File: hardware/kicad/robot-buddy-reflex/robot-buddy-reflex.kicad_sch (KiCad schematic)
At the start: 23 parts, among them J1 Motor A, J2 Motor B, J5 Qwiic, J6 HC-SR04, J7 E-Stop, J8 PWR In, J9 UART/Pi, U1 Waveshare_ESP32-S3-Zero, U2 SparkFun_TB6612FNG_v2

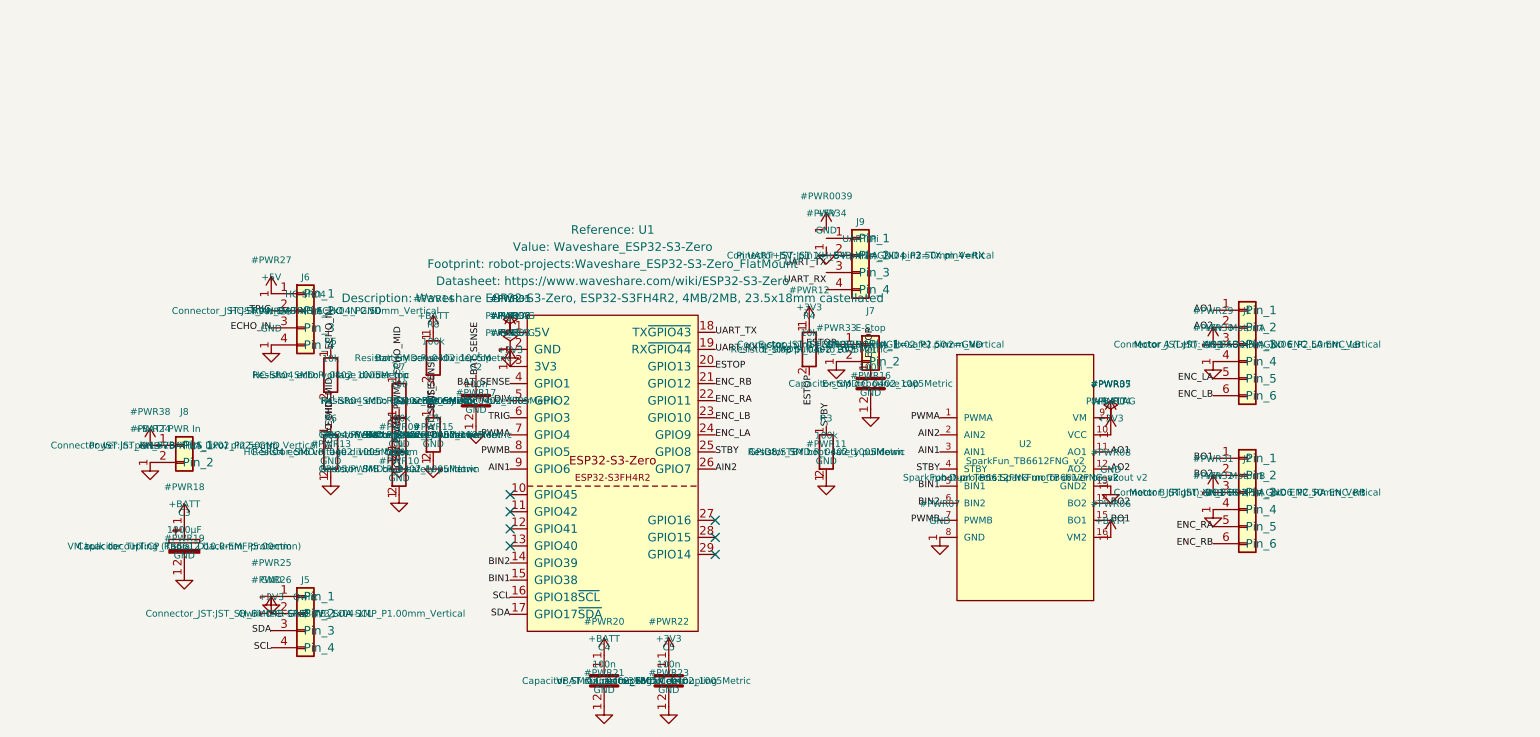
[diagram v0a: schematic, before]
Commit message: schematic: add J10 power LED, J11 NeoPixel, U3 level-shift circuit
J10 (XH 2-pin): panel-mount power LED hardwired to +5V rail via R10
(330Ω) — always on when powered, no GPIO dependency.

J11 (XH 3-pin): WS2812B NeoPixel DATA/+5V/GND. Data driven by GPIO42
(inner cluster pad 11) through U3 (74LVC1G125 SOT-23-5), which
level-shifts 3.3V→5V to meet WS2812B Vih. R11 (330Ω) suppresses
ringing on the 800kHz data line. C6 (100µF) + C7 (100nF) decouple the
5V rail at the connector against 64-LED inrush.
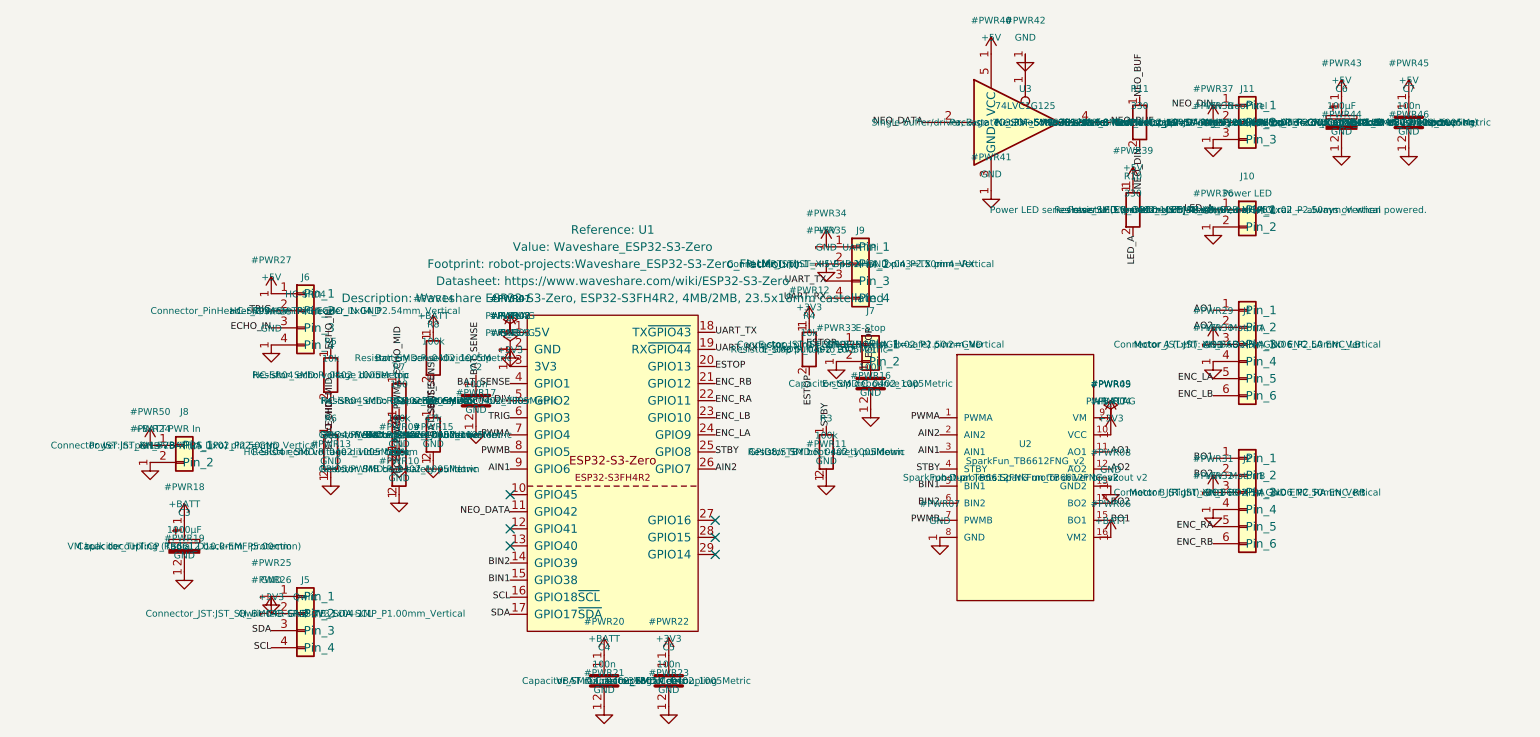
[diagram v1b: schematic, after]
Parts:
- added C6: 100µF, Capacitor_THT:CP_Radial_D5.0mm_P2.50mm, symbol Device:C_Polarized
- added C7: 100n, Capacitor_SMD:C_0402_1005Metric, symbol Device:C
- added J10: Power LED, Connector_JST:JST_XH_B2B-XH-A_1x02_P2.50mm_Vertical, symbol Connector_Generic:Conn_01x02
- added J11: NeoPixel, Connector_JST:JST_XH_B3B-XH-A_1x03_P2.50mm_Vertical, symbol Connector_Generic:Conn_01x03
- added R10, R11: 330, Resistor_SMD:R_0402_1005Metric, symbol Device:R
- added U3: 74LVC1G125, Package_TO_SOT_SMD:SOT-23-5, symbol 74xGxx:74LVC1G125
- J6: footprint Connector_JST:JST_XH_B4B-XH-A_1x04_P2.50mm_Vertical -> Connector_PinHeader_2.54mm:PinHeader_1x04_P2.54mm_Vertical
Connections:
- net +5V: now also J9.1 (Pin_1), C6.1, C7.1, J11.2 (Pin_2), R10.1, U3.5 (VCC)
- net GND: now also J9.2 (Pin_2), C6.2, C7.2, J10.2 (Pin_2), J11.3 (Pin_3), U3.1, U3.3 (GND)
- net UART_RX: now also J9.4 (Pin_4)
- net UART_TX: now also J9.3 (Pin_3)
- net NEO_DATA: now reaches U1.11 (GPIO42)
- net NEO_DATA: now also U3.2
- new net LED_A: J10.1 (Pin_1), R10.2
- new net NEO_BUF: R11.1, U3.4
- new net NEO_DIN: J11.1 (Pin_1), R11.2
- no-connect marks 7 -> 6

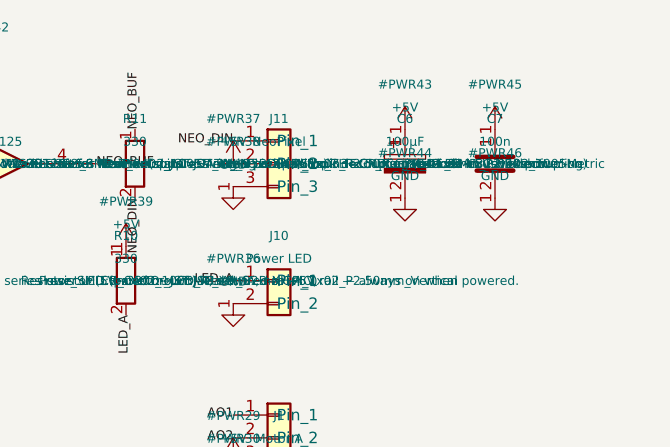
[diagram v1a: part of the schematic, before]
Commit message: hardware: fix C6 NeoPixel bulk cap footprint to P2.00mm
EEU-FM1A101 has 2.00mm lead spacing; P2.50mm would have been wrong.
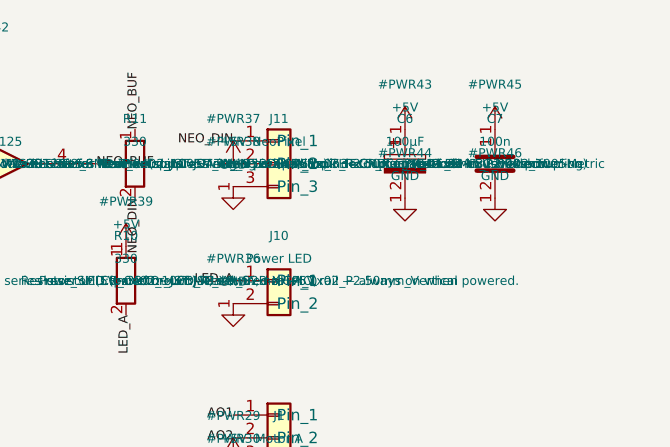
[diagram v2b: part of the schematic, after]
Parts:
- C6: footprint Capacitor_THT:CP_Radial_D5.0mm_P2.50mm -> Capacitor_THT:CP_Radial_D5.0mm_P2.00mm
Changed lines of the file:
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@@
       (effects (font (size 1.0 1.0)))
     )
-    (property "Footprint" "Capacitor_THT:CP_Radial_D5.0mm_P2.50mm" (at 262.0 45.0 0)
+    (property "Footprint" "Capacitor_THT:CP_Radial_D5.0mm_P2.00mm" (at 262.0 45.0 0)
       (effects (font (size 1.0 1.0)))
     )
